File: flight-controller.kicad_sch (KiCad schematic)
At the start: 3 parts

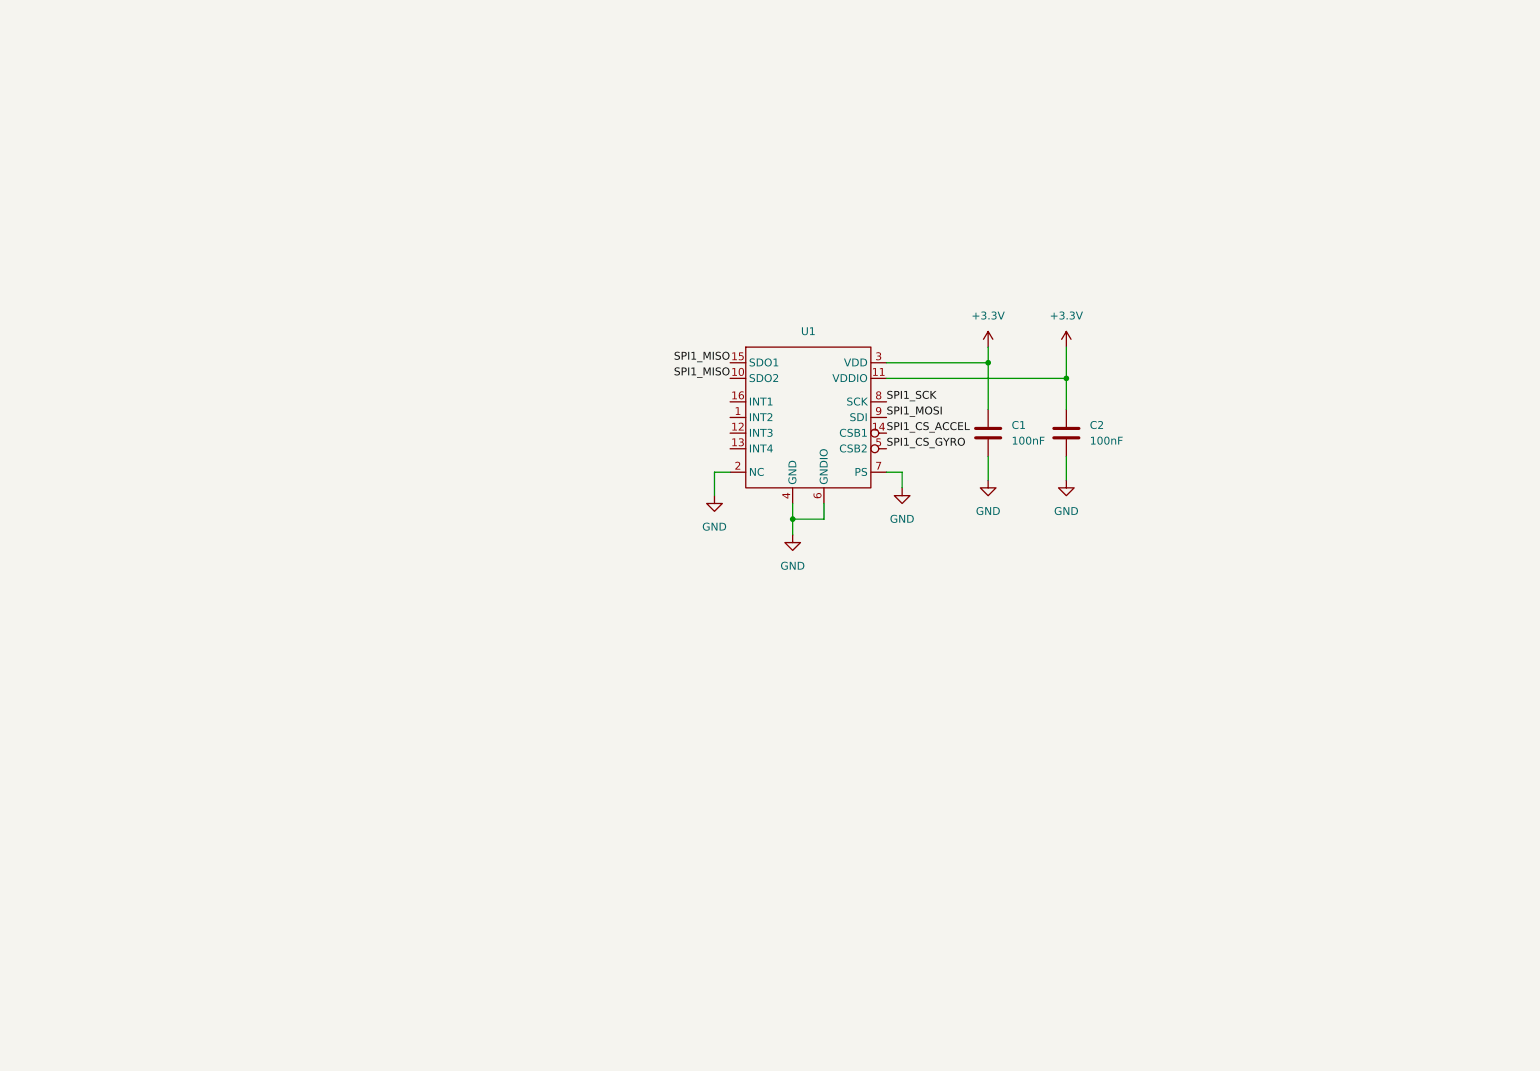
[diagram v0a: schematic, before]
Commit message: feat: Added stm32 header connectors
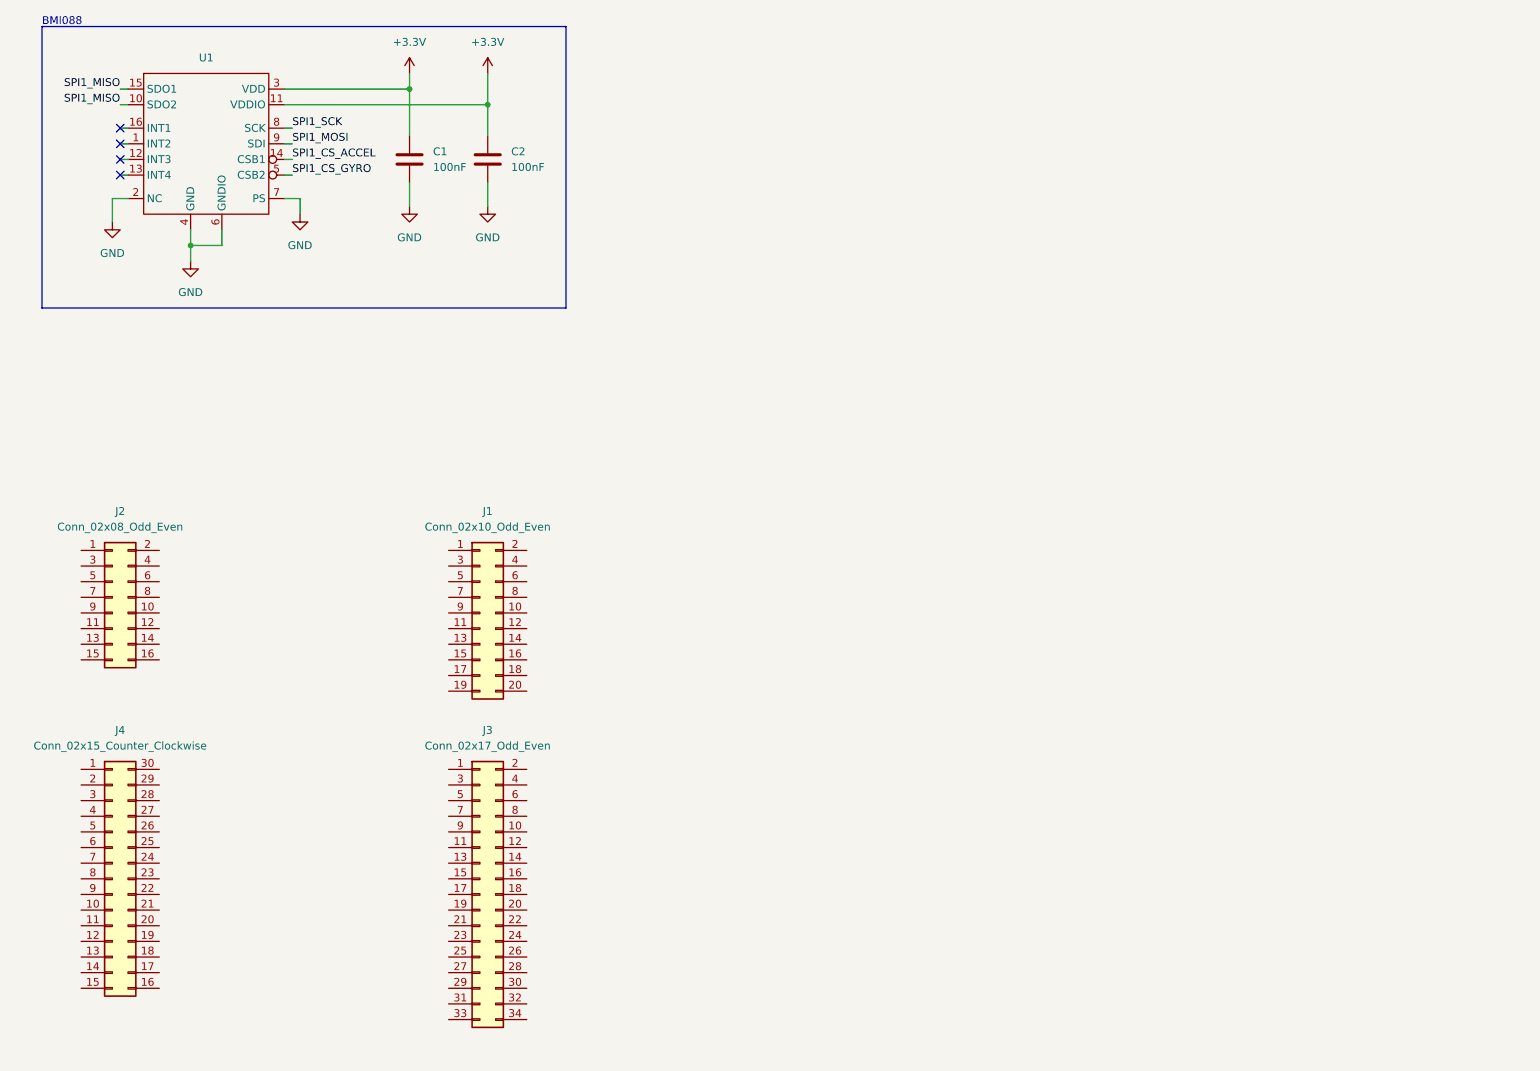
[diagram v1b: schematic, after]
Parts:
- added J1: Conn_02x10_Odd_Even, symbol Connector_Generic:Conn_02x10_Odd_Even
- added J2: Conn_02x08_Odd_Even, symbol Connector_Generic:Conn_02x08_Odd_Even
- added J3: Conn_02x17_Odd_Even, symbol Connector_Generic:Conn_02x17_Odd_Even
- added J4: Conn_02x15_Counter_Clockwise, symbol Connector_Generic:Conn_02x15_Counter_Clockwise
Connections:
- no-connect marks 0 -> 4
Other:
- note added: "BMI088"
- moved on the sheet: C1, C2, U1

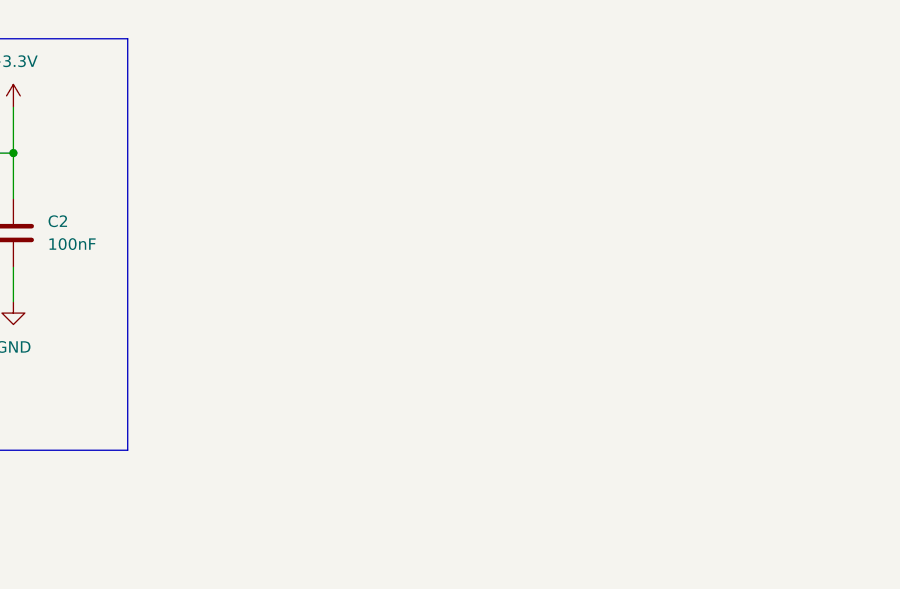
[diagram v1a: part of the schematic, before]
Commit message: feat: Added bmp390 to main schematic
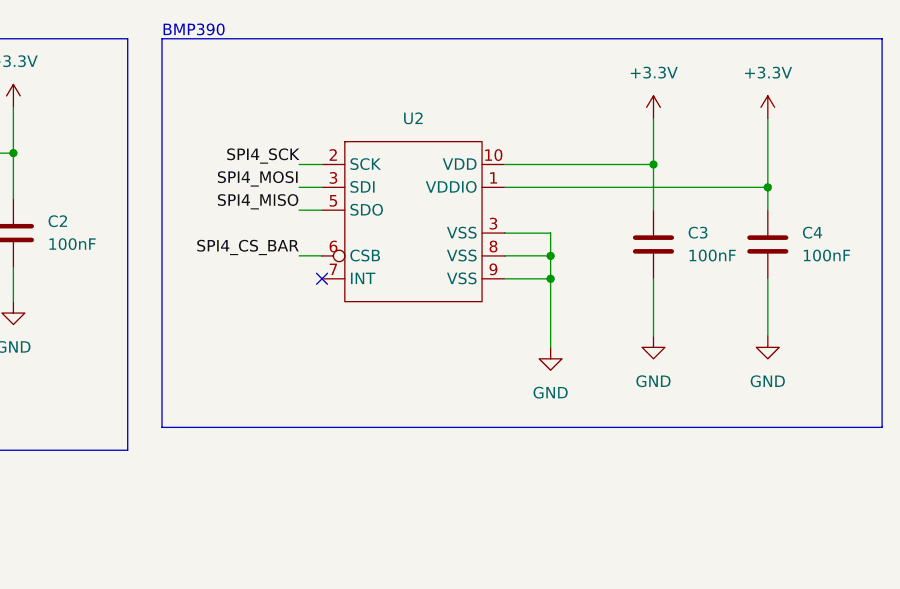
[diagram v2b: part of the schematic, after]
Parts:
- added C3, C4: 100nF, symbol Device:C
- added U2: ~, symbol fc_custom:BMP390
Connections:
- net +3.3V: now also C3.1, C4.1, U2.1 (VDDIO), U2.10 (VDD)
- net GND: now also C3.2, C4.2, U2.3 (VSS), U2.8 (VSS), U2.9 (VSS)
- new net SPI4_CS_BAR: U2.6 (CSB)
- new net SPI4_MISO: U2.5 (SDO)
- new net SPI4_MOSI: U2.3 (VSS)
- new net SPI4_SCK: U2.2 (SCK)
- no-connect marks 4 -> 5
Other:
- note added: "BMP390"

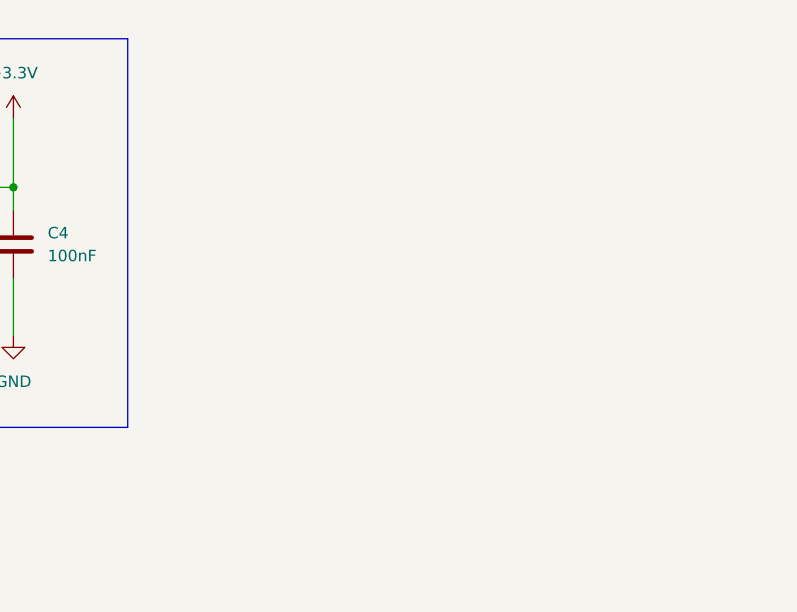
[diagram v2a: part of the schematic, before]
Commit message: feat: Added ACS773 sensor
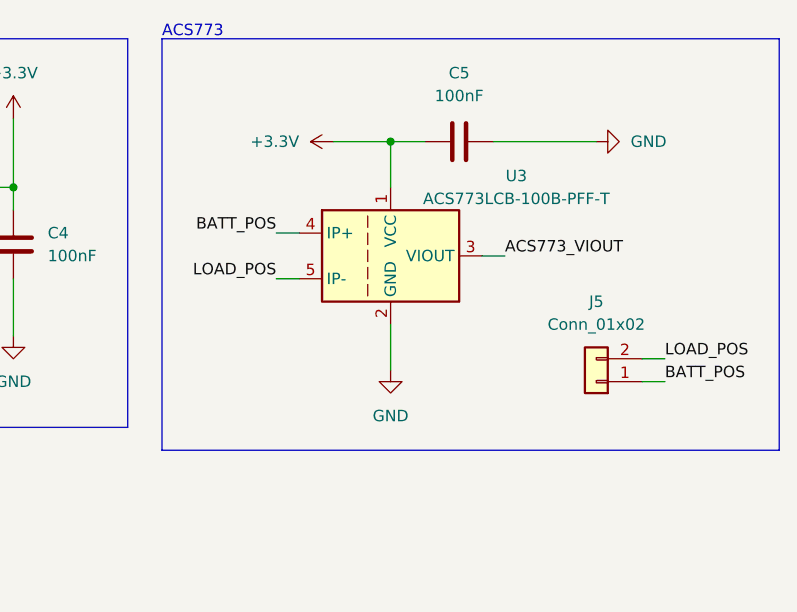
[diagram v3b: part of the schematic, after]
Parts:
- added C5: 100nF, symbol Device:C
- added J5: Conn_01x02, symbol Connector_Generic:Conn_01x02
- added U3: ACS773LCB-100B-PFF-T, Sensor_Current:Allegro_CB_PFF, symbol Sensor_Current:ACS770xCB-100B-PFF
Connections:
- net +3.3V: now also C5.1, U3.1 (VCC)
- net GND: now also C5.2, U3.2 (GND)
- new net ACS773_VIOUT: U3.3 (VIOUT)
- new net BATT_POS: J5.1 (Pin_1), U3.4 (IP+)
- new net LOAD_POS: J5.2 (Pin_2), U3.5 (IP-)
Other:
- note added: "ACS773"
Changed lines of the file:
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@@
   (junction (at 93.98 36.83) (diameter 0) (color 0 0 0 0)
+  )
+  (junction (at 219.71 35.56) (diameter 0) (color 0 0 0 0)
   )
   (junction (at 81.28 34.29) (diameter 0) (color 0 0 0 0)
@@
     (stroke (width 0) (type default))
   )
+  (wire (pts (xy 213.36 35.56) (xy 219.71 35.56))
+    (stroke (width 0) (type default))
+  )
+  (wire (pts (xy 219.71 55.88) (xy 219.71 60.96))
+    (stroke (width 0) (type default))
+  )
+  (wire (pts (xy 219.71 35.56) (xy 219.71 40.64))
+    (stroke (width 0) (type default))
+  )
+  (wire (pts (xy 207.01 50.8) (xy 209.55 50.8))
+    (stroke (width 0) (type default))
+  )
   (wire (pts (xy 165.1 50.8) (xy 165.1 57.15))
     (stroke (width 0) (type default))
@@
     (stroke (width 0) (type default))
   )
+  (wire (pts (xy 219.71 35.56) (xy 223.52 35.56))
+    (stroke (width 0) (type default))
+  )
   (wire (pts (xy 148.59 38.1) (xy 165.1 38.1))
     (stroke (width 0) (type default))
@@
     (stroke (width 0) (type default))
   )
+  (wire (pts (xy 229.87 48.26) (xy 232.41 48.26))
+    (stroke (width 0) (type default))
+  )
   (wire (pts (xy 81.28 34.29) (xy 81.28 41.91))
     (stroke (width 0) (type default))
@@
     (stroke (width 0) (type default))
   )
+  (wire (pts (xy 207.01 45.72) (xy 209.55 45.72))
+    (stroke (width 0) (type default))
+  )
   (wire (pts (xy 153.67 48.26) (xy 153.67 50.8))
     (stroke (width 0) (type default))
@@
     (stroke (width 0) (type default))
   )
+  (wire (pts (xy 231.14 35.56) (xy 242.57 35.56))
+    (stroke (width 0) (type default))
+  )
   (wire (pts (xy 62.23 45.72) (xy 60.96 45.72))
     (stroke (width 0) (type default))
@@
     (stroke (width 0) (type default))
   )
+  (wire (pts (xy 247.65 59.69) (xy 250.19 59.69))
+    (stroke (width 0) (type default))
+  )
   (wire (pts (xy 62.23 48.26) (xy 60.96 48.26))
     (stroke (width 0) (type default))
@@
     (stroke (width 0) (type default))
   )
+  (wire (pts (xy 247.65 62.23) (xy 250.19 62.23))
+    (stroke (width 0) (type default))
+  )
   (wire (pts (xy 93.98 49.53) (xy 93.98 53.34))
     (stroke (width 0) (type default))
@@
     (stroke (width 0) (type default))
     (fill (type none))
+  )
+  (rectangle (start 194.31 24.13) (end 262.89 69.85)
+    (stroke (width 0) (type default))
+    (fill (type none))
+  )
+  (text "ACS773" (at 194.31 24.13 0)
+    (effects (font (size 1.27 1.27)) (justify left bottom))
   )
   (text "BMI088" (at 21.59 24.13 0)
@@
     (effects (font (size 1.27 1.27)) (justify right bottom))
   )
+  (label "ACS773_VIOUT" (at 232.41 48.26 0) (fields_autoplaced)
+    (effects (font (size 1.27 1.27)) (justify left bottom))
+  )
+  (label "LOAD_POS" (at 250.19 59.69 0) (fields_autoplaced)
+    (effects (font (size 1.27 1.27)) (justify left bottom))
+  )
   (label "SPI1_MOSI" (at 62.23 43.18 0) (fields_autoplaced)
     (effects (font (size 1.27 1.27)) (justify left bottom))
   )
+  (label "LOAD_POS" (at 207.01 50.8 180) (fields_autoplaced)
+    (effects (font (size 1.27 1.27)) (justify right bottom))
+  )
   (label "SPI4_MISO" (at 125.73 43.18 180) (fields_autoplaced)
     (effects (font (size 1.27 1.27)) (justify right bottom))
@@
     (effects (font (size 1.27 1.27)) (justify right bottom))
   )
+  (label "BATT_POS" (at 250.19 62.23 0) (fields_autoplaced)
+    (effects (font (size 1.27 1.27)) (justify left bottom))
+  )
   (label "SPI1_MISO" (at 34.29 34.29 180) (fields_autoplaced)
     (effects (font (size 1.27 1.27)) (justify right bottom))
@@
   )
   (label "SPI1_MISO" (at 34.29 36.83 180) (fields_autoplaced)
+    (effects (font (size 1.27 1.27)) (justify right bottom))
+  )
+  (label "BATT_POS" (at 207.01 45.72 180) (fields_autoplaced)
     (effects (font (size 1.27 1.27)) (justify right bottom))
   )
@@
         (path "/1e8bc6c3-9c25-4744-8bc3-112c39d50b38"
           (reference "J2") (unit 1)
+        )
+      )
+    )
+  )
+  (symbol (lib_id "Device:C") (at 227.33 35.56 90) (unit 1)
+    (in_bom yes) (on_board yes) (dnp no) (fields_autoplaced)
+    (property "Reference" "C5" (at 227.33 27.94 90)
+      (effects (font (size 1.27 1.27)))
+    )
+    (property "Value" "100nF" (at 227.33 30.48 90)
+      (effects (font (size 1.27 1.27)))
+    )
+    (property "Footprint" "" (at 231.14 34.5948 0)
+      (effects (font (size 1.27 1.27)) hide)
+    )
+    (property "Datasheet" "~" (at 227.33 35.56 0)
+      (effects (font (size 1.27 1.27)) hide)
+    )
+    (pin "2")
+    (pin "1")
+    (instances
+      (project "flight-controller"
+        (path "/1e8bc6c3-9c25-4744-8bc3-112c39d50b38"
+          (reference "C5") (unit 1)
+        )
+      )
+    )
+  )
+  (symbol (lib_id "Connector_Generic:Conn_01x02") (at 242.57 62.23 180) (unit 1)
+    (in_bom yes) (on_board yes) (dnp no) (fields_autoplaced)
+    (property "Reference" "J5" (at 242.57 53.34 0)
+      (effects (font (size 1.27 1.27)))
+    )
+    (property "Value" "Conn_01x02" (at 242.57 55.88 0)
+      (effects (font (size 1.27 1.27)))
+    )
+    (property "Footprint" "" (at 242.57 62.23 0)
+      (effects (font (size 1.27 1.27)) hide)
+    )
+    (property "Datasheet" "~" (at 242.57 62.23 0)
+      (effects (font (size 1.27 1.27)) hide)
+    )
+    (pin "1")
+    (pin "2")
+    (instances
+      (project "flight-controller"
+        (path "/1e8bc6c3-9c25-4744-8bc3-112c39d50b38"
+          (reference "J5") (unit 1)
         )
       )
@@
         (path "/1e8bc6c3-9c25-4744-8bc3-112c39d50b38"
           (reference "J4") (unit 1)
+        )
+      )
+    )
+  )
+  (symbol (lib_id "power:GND") (at 219.71 60.96 0) (unit 1)
+    (in_bom yes) (on_board yes) (dnp no) (fields_autoplaced)
+    (property "Reference" "#PWR015" (at 219.71 67.31 0)
+      (effects (font (size 1.27 1.27)) hide)
+    )
+    (property "Value" "GND" (at 219.71 66.04 0)
+      (effects (font (size 1.27 1.27)))
+    )
+    (property "Footprint" "" (at 219.71 60.96 0)
+      (effects (font (size 1.27 1.27)) hide)
+    )
+    (property "Datasheet" "" (at 219.71 60.96 0)
+      (effects (font (size 1.27 1.27)) hide)
+    )
+    (pin "1")
+    (instances
+      (project "flight-controller"
+        (path "/1e8bc6c3-9c25-4744-8bc3-112c39d50b38"
+          (reference "#PWR015") (unit 1)
         )
       )
@@
     )
   )
+  (symbol (lib_id "power:+3.3V") (at 213.36 35.56 90) (unit 1)
+    (in_bom yes) (on_board yes) (dnp no) (fields_autoplaced)
+    (property "Reference" "#PWR013" (at 217.17 35.56 0)
+      (effects (font (size 1.27 1.27)) hide)
+    )
+    (property "Value" "+3.3V" (at 209.55 35.56 90)
+      (effects (font (size 1.27 1.27)) (justify left))
+    )
+    (property "Footprint" "" (at 213.36 35.56 0)
+      (effects (font (size 1.27 1.27)) hide)
+    )
+    (property "Datasheet" "" (at 213.36 35.56 0)
+      (effects (font (size 1.27 1.27)) hide)
+    )
+    (pin "1")
+    (instances
+      (project "flight-controller"
+        (path "/1e8bc6c3-9c25-4744-8bc3-112c39d50b38"
+          (reference "#PWR013") (unit 1)
+        )
+      )
+    )
+  )
   (symbol (lib_id "power:GND") (at 93.98 53.34 0) (unit 1)
     (in_bom yes) (on_board yes) (dnp no) (fields_autoplaced)
@@
         (path "/1e8bc6c3-9c25-4744-8bc3-112c39d50b38"
           (reference "#PWR05") (unit 1)
+        )
+      )
+    )
+  )
+  (symbol (lib_id "power:GND") (at 242.57 35.56 90) (unit 1)
+    (in_bom yes) (on_board yes) (dnp no) (fields_autoplaced)
+    (property "Reference" "#PWR014" (at 248.92 35.56 0)
+      (effects (font (size 1.27 1.27)) hide)
+    )
+    (property "Value" "GND" (at 246.38 35.56 90)
+      (effects (font (size 1.27 1.27)) (justify right))
+    )
+    (property "Footprint" "" (at 242.57 35.56 0)
+      (effects (font (size 1.27 1.27)) hide)
+    )
+    (property "Datasheet" "" (at 242.57 35.56 0)
+      (effects (font (size 1.27 1.27)) hide)
+    )
+    (pin "1")
+    (instances
+      (project "flight-controller"
+        (path "/1e8bc6c3-9c25-4744-8bc3-112c39d50b38"
+          (reference "#PWR014") (unit 1)
         )
       )
@@
         )
       )
+    )
+  )
+  (symbol (lib_id "Sensor_Current:ACS770xCB-100B-PFF") (at 219.71 48.26 0) (unit 1)
+    (in_bom yes) (on_board yes) (dnp no)
+    (property "Reference" "U3" (at 233.68 39.37 0)
+      (effects (font (size 1.27 1.27)))
+    )
+    (property "Value" "ACS773LCB-100B-PFF-T" (at 233.68 41.91 0)
+      (effects (font (size 1.27 1.27)))
+    )
+    (property "Footprint" "Sensor_Current:Allegro_CB_PFF" (at 219.71 48.26 0)
+      (effects (font (size 1.27 1.27)) hide)
+    )
+    (property "Datasheet" "https://www.allegromicro.com/~/media/files/datasheets/acs773-datasheet.pdf" (at 219.71 48.26 0)
+      (effects (font (size 1.27 1.27)) hide)
+    )
+    (pin "3")
+    (pin "2")
+    (pin "1")
+    (pin "4")
+    (pin "5")
+    (instances
+      (project "flight-controller"
+        (path "/1e8bc6c3-9c25-4744-8bc3-112c39d50b38"
+          (reference "U3") (unit 1)
+        )
+      )
